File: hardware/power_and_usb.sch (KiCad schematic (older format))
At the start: 49 parts

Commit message: Annotation complete
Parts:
- gave numbers to parts that had none: 49

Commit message: Finish adding footprints
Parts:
- BT1, TH1: footprint (none) -> libs:DG142R-5.08-02P-14
- C19, C20, C23, C24, C26, C28, C29, C30, C31, C32, C33, C34: footprint (none) -> Capacitor_SMD:C_0805_2012Metric
- C21, C22, C25, C27: footprint (none) -> Capacitor_SMD:C_1206_3216Metric
- D1: footprint (none) -> LED_SMD:LED_0603_1608Metric
- J2: footprint MOLEX_105450-0101 -> libs:105450-0101
- JP2: footprint (none) -> Connector_PinHeader_2.54mm:PinHeader_1x02_P2.54mm_Vertical
- L3: footprint (none) -> Inductor_SMD:L_1008_2520Metric
- R24, R25, R26, R29, R30, R31, R32, R33, R34, R35, R38, R39, R40, R41, R42: footprint (none) -> Resistor_SMD:R_0805_2012Metric
- R27, R37, R43, R44: footprint (none) -> Resistor_SMD:R_2512_6332Metric
- R28: value 260R -> 200R; footprint (none) -> Resistor_SMD:R_0805_2012Metric
- R36: value 200R -> 100R; footprint (none) -> Resistor_SMD:R_0805_2012Metric
- SW2: footprint (none) -> libs:SW_TS-1187A-B-A-B

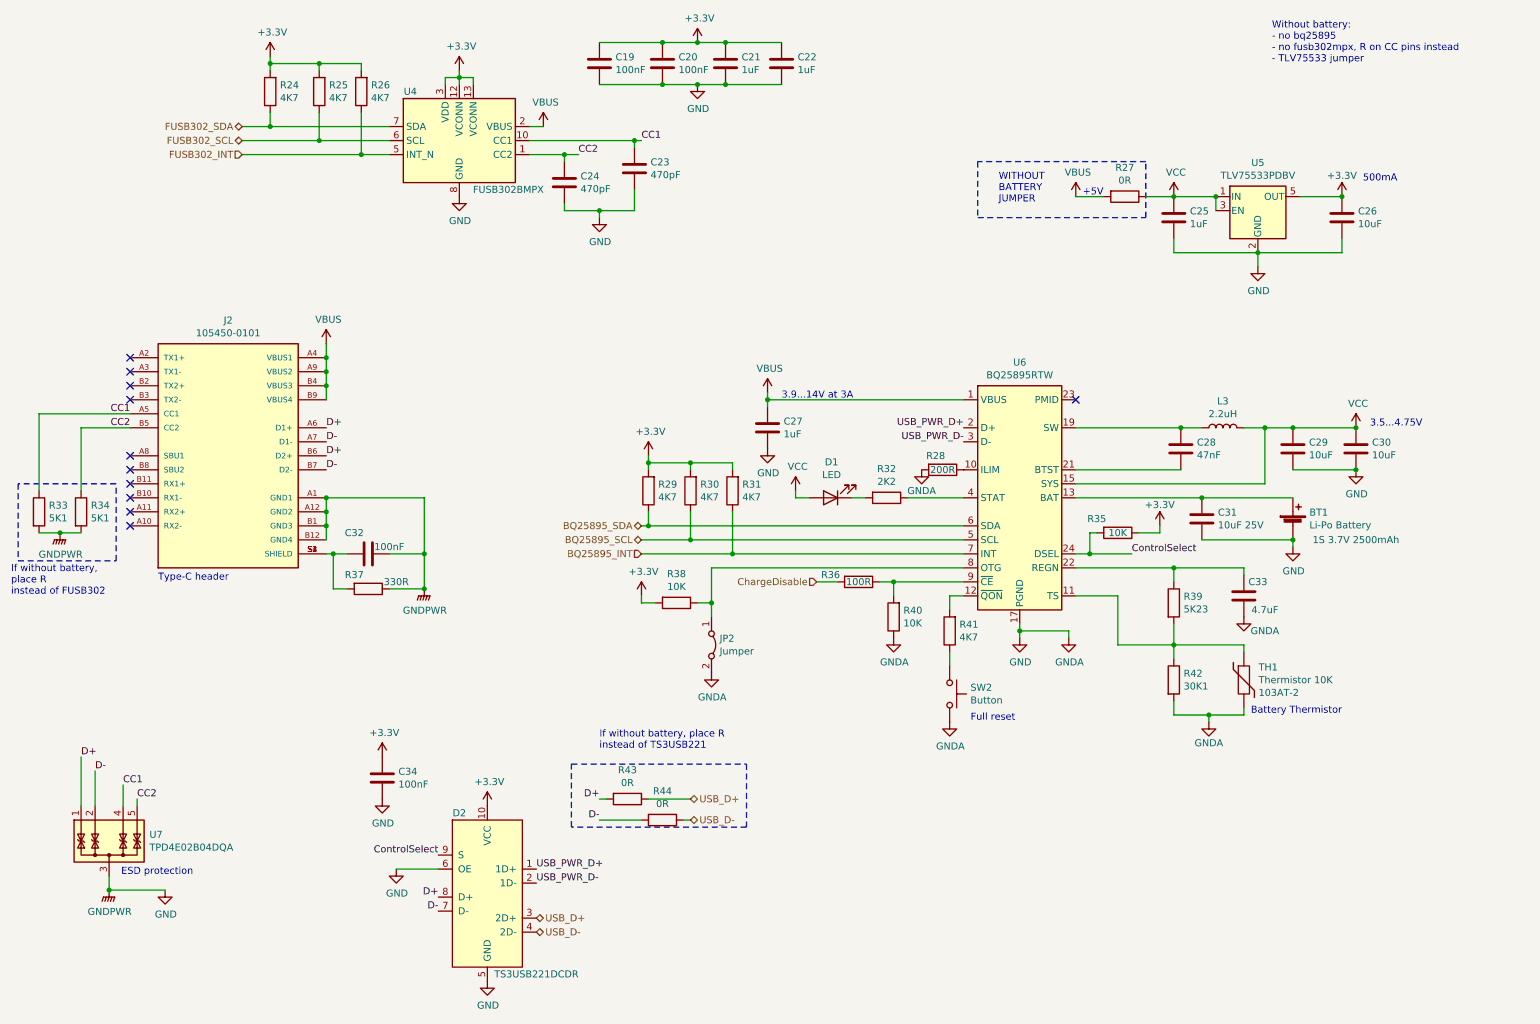
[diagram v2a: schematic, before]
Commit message: Change 0Rto solder jumpers Add 3d model for bq25895 Fix button pcb model Start power part of pcb
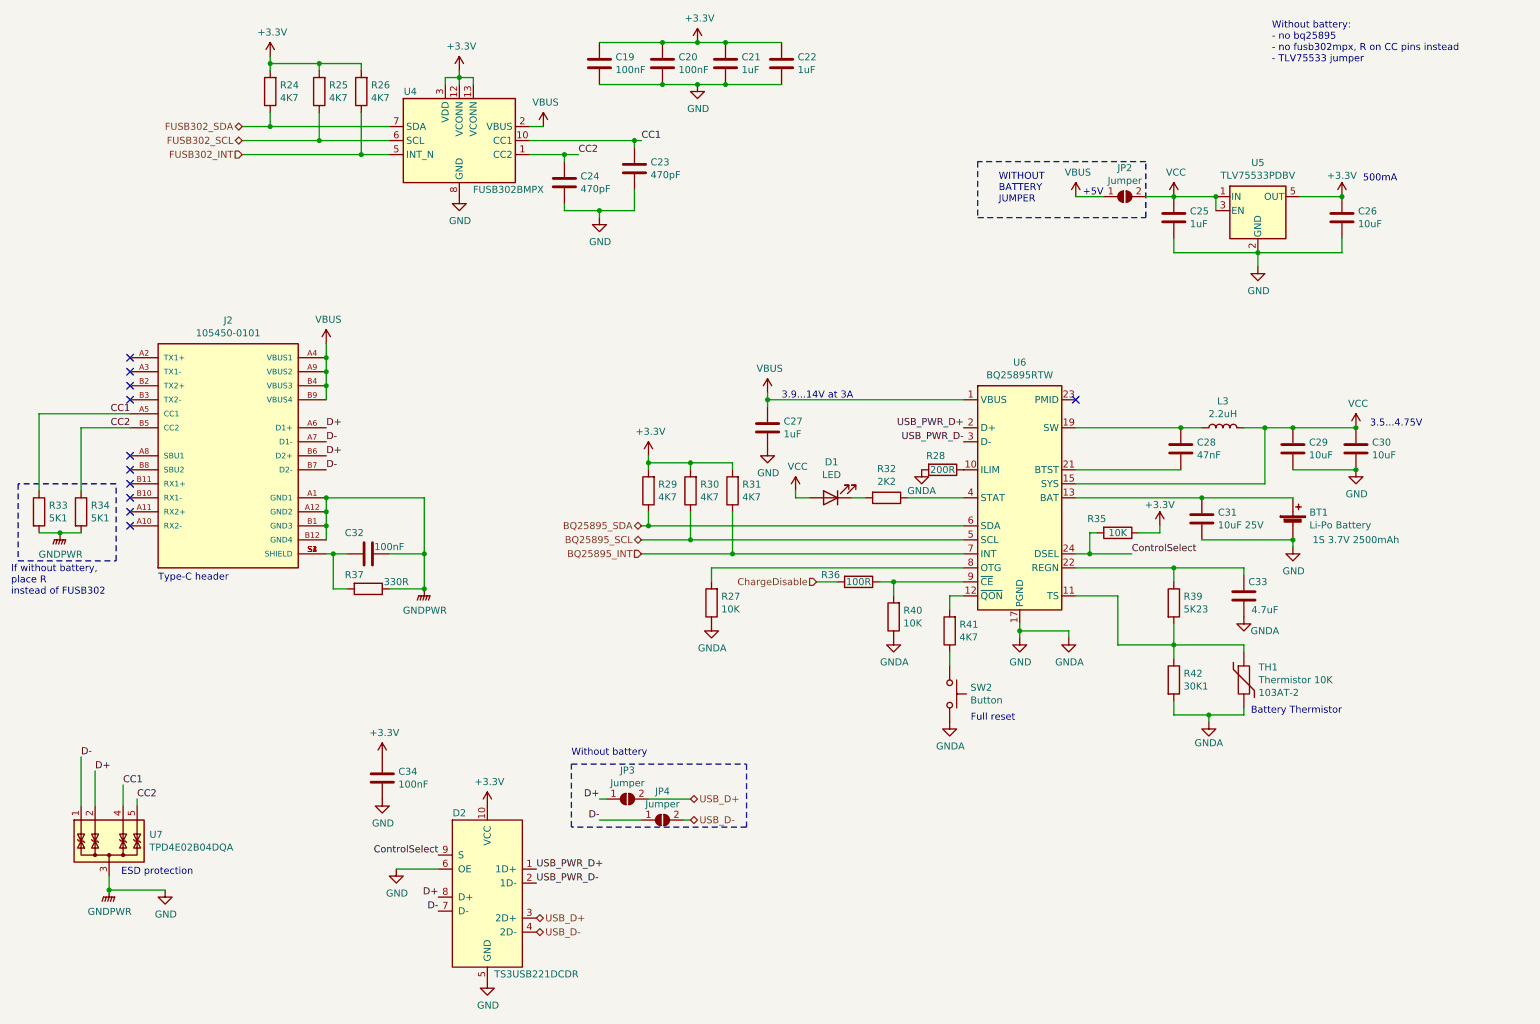
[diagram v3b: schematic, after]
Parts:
- removed JP2: Jumper, Connector_PinHeader_2.54mm:PinHeader_1x02_P2.54mm_Vertical, symbol Jumper:Jumper_2_Bridged
- removed R38: 10K, Resistor_SMD:R_0805_2012Metric, symbol Device:R
- removed R43, R44: 0R, Resistor_SMD:R_2512_6332Metric, symbol Device:R
- added JP2, JP3, JP4: Jumper, Jumper:SolderJumper-2_P1.3mm_Open_TrianglePad1.0x1.5mm, symbol Jumper:SolderJumper_2_Open
- R27: value 0R -> 10K; footprint Resistor_SMD:R_2512_6332Metric -> Resistor_SMD:R_0805_2012Metric
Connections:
- net D+: now also U7.2 (IO2), JP3.1 (A); no longer U7.1 (IO1)
- net D-: now also U7.1 (IO1), JP4.1 (A); no longer U7.2 (IO2)
- net GND: now also R27.1
- net USB_D+: now also JP3.2 (B)
- net USB_D-: now also JP4.2 (B)
- net VBUS: now also JP2.1 (A); no longer R27.2
- net VCC: now also JP2.2 (B); no longer R27.1
- net at U6.8 (OTG): now also R27.2
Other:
- note added: "Without battery"
- note removed: "If without battery, place R \ninstead of TS3USB221"
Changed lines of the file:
@@
 Text Notes 1800 6700 2    50   ~ 0
 ESD protection
+Text Label 1100 5950 0    50   ~ 0
+D+
 Text Label 1000 5850 0    50   ~ 0
-D+
-Text Label 1100 5950 0    50   ~ 0
 D-
 Text Label 1300 6050 0    50   ~ 0
@@
 U 1 1 60501F6D
 P 3900 6850
+AR Path="/60501F6D" Ref="D2"  Part="1"
+AR Path="/603656E0/60501F6D" Ref="D2"  Part="1"
 F 0 "D2" H 3700 7450 50  0000 C CNN
 F 1 "TS3USB221DCDR" H 4250 6300 50  0000 C CNN
@@
 L power:GNDA #PWR073
 U 1 1 605D7733
-P 5500 5250
-F 0 "#PWR073" H 5500 5000 50  0001 C CNN
-F 1 "GNDA" H 5505 5077 50  0000 C CNN
-F 2 "" H 5500 5250 50  0001 C CNN
-F 3 "" H 5500 5250 50  0001 C CNN
-	1    5500 5250
+P 5500 4900
+F 0 "#PWR073" H 5500 4650 50  0001 C CNN
+F 1 "GNDA" H 5505 4727 50  0000 C CNN
+F 2 "" H 5500 4900 50  0001 C CNN
+F 3 "" H 5500 4900 50  0001 C CNN
+	1    5500 4900
 	1    0    0    -1
 $EndComp
@@
 	1    8100 1850
 	1    0    0    -1
-$EndComp
-$Comp
-L Device:R R27
-U 1 1 606CDF7A
-P 8450 1850
-F 0 "R27" V 8243 1850 50  0000 C CNN
-F 1 "0R" V 8334 1850 50  0000 C CNN
-F 2 "Resistor_SMD:R_2512_6332Metric" V 8380 1850 50  0001 C CNN
-F 3 "~" H 8450 1850 50  0001 C CNN
-	1    8450 1850
-	0    1    1    0
 $EndComp
 Wire Wire Line
@@
 Text Label 4700 6300 2    50   ~ 0
 D-
-$Comp
-L Device:R R43
-U 1 1 60734F94
-P 4900 6150
-F 0 "R43" V 4693 6150 50  0000 C CNN
-F 1 "0R" V 4784 6150 50  0000 C CNN
-F 2 "Resistor_SMD:R_2512_6332Metric" V 4830 6150 50  0001 C CNN
-F 3 "~" H 4900 6150 50  0001 C CNN
-	1    4900 6150
-	0    1    1    0
-$EndComp
-$Comp
-L Device:R R44
-U 1 1 60737243
-P 5150 6300
-F 0 "R44" V 4943 6300 50  0000 C CNN
-F 1 "0R" V 5034 6300 50  0000 C CNN
-F 2 "Resistor_SMD:R_2512_6332Metric" V 5080 6300 50  0001 C CNN
-F 3 "~" H 5150 6300 50  0001 C CNN
-	1    5150 6300
-	0    1    1    0
-$EndComp
 Wire Wire Line
 	5300 6300 5350 6300
@@
 Wire Notes Line
 	4500 6350 4500 5900
-Text Notes 4700 5800 0    50   ~ 0
-If without battery, place R \ninstead of TS3USB221
+Text Notes 4500 5850 0    50   ~ 0
+Without battery
 Text Notes 9350 5550 0    50   ~ 0
 Battery Thermistor
@@
 Wire Wire Line
 	7300 4500 5500 4500
-$Comp
-L Jumper:Jumper_2_Bridged JP2
-U 1 1 60885D87
-P 5500 5050
-F 0 "JP2" V 5454 5108 50  0000 L CNN
-F 1 "Jumper" V 5545 5108 50  0000 L CNN
-F 2 "Connector_PinHeader_2.54mm:PinHeader_1x02_P2.54mm_Vertical" H 5500 5050 50  0001 C CNN
-F 3 "~" H 5500 5050 50  0001 C CNN
-	1    5500 5050
-	0    1    1    0
-$EndComp
-$Comp
-L Device:R R38
-U 1 1 6088DE66
-P 5250 4750
-F 0 "R38" V 5043 4750 50  0000 C CNN
-F 1 "10K" V 5134 4750 50  0000 C CNN
-F 2 "Resistor_SMD:R_0805_2012Metric" V 5180 4750 50  0001 C CNN
-F 3 "~" H 5250 4750 50  0001 C CNN
-	1    5250 4750
-	0    1    1    0
-$EndComp
-Wire Wire Line
-	5500 4500 5500 4750
-Wire Wire Line
-	5400 4750 5500 4750
-Connection ~ 5500 4750
-Wire Wire Line
-	5500 4750 5500 4850
-$Comp
-L power:+3.3V #PWR068
-U 1 1 608A3905
-P 5000 4700
-F 0 "#PWR068" H 5000 4550 50  0001 C CNN
-F 1 "+3.3V" H 5015 4873 50  0000 C CNN
-F 2 "" H 5000 4700 50  0001 C CNN
-F 3 "" H 5000 4700 50  0001 C CNN
-	1    5000 4700
-	1    0    0    -1
-$EndComp
-Wire Wire Line
-	5000 4700 5000 4750
-Wire Wire Line
-	5000 4750 5100 4750
 Wire Wire Line
 	5050 3800 5050 3750
@@
 	2350 900  2350 850
 Connection ~ 2350 900
+$Comp
+L Jumper:SolderJumper_2_Open JP3
+U 1 1 608D23C1
+P 4900 6150
+F 0 "JP3" H 4900 6355 50  0000 C CNN
+F 1 "Jumper" H 4900 6264 50  0000 C CNN
+F 2 "Jumper:SolderJumper-2_P1.3mm_Open_TrianglePad1.0x1.5mm" H 4900 6150 50  0001 C CNN
+F 3 "~" H 4900 6150 50  0001 C CNN
+	1    4900 6150
+	1    0    0    -1
+$EndComp
+$Comp
+L Jumper:SolderJumper_2_Open JP4
+U 1 1 608D4957
+P 5150 6300
+F 0 "JP4" H 5150 6505 50  0000 C CNN
+F 1 "Jumper" H 5150 6414 50  0000 C CNN
+F 2 "Jumper:SolderJumper-2_P1.3mm_Open_TrianglePad1.0x1.5mm" H 5150 6300 50  0001 C CNN
+F 3 "~" H 5150 6300 50  0001 C CNN
+	1    5150 6300
+	1    0    0    -1
+$EndComp
+Wire Wire Line
+	5500 4500 5500 4600
+$Comp
+L Device:R R27
+U 1 1 608D9844
+P 5500 4750
+F 0 "R27" H 5430 4704 50  0000 R CNN
+F 1 "10K" H 5430 4795 50  0000 R CNN
+F 2 "Resistor_SMD:R_0805_2012Metric" V 5430 4750 50  0001 C CNN
+F 3 "~" H 5500 4750 50  0001 C CNN
+	1    5500 4750
+	-1   0    0    1
+$EndComp
+$Comp
+L Jumper:SolderJumper_2_Open JP2
+U 1 1 608DB3E1
+P 8450 1850
+F 0 "JP2" H 8450 2055 50  0000 C CNN
+F 1 "Jumper" H 8450 1964 50  0000 C CNN
+F 2 "Jumper:SolderJumper-2_P1.3mm_Open_TrianglePad1.0x1.5mm" H 8450 1850 50  0001 C CNN
+F 3 "~" H 8450 1850 50  0001 C CNN
+	1    8450 1850
+	1    0    0    -1
+$EndComp
 $EndSCHEMATC
